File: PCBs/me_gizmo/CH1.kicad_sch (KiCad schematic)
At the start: 10 parts, among them J1 PushButton_Terminal_01x06, U1 ADG714, U2 ADG714, U3 ADG714

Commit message: Completed first draft of integrated measurement unit
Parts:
- removed U2: ADG714, Package_SO:TSSOP-24_4.4x7.8mm_P0.65mm, symbol Analog_Switch:ADG714
- added U2: ADG714, Package_SO:TSSOP-24_4.4x7.8mm_P0.65mm, symbol Analog_Switch:ADG714
- J1: footprint WAGO:CONN5_233-505_WAG -> TerminalBlock_WAGO:TerminalBlock_WAGO_233-506_2x06_P2.54mm
- R4, R7, R8: value 348 -> 348Ω
- R5, R6, R9: value 118 -> 118Ω
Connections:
- net ADC1+: now also U3.5 (S); no longer J1.5 (Pin_5), U3.6 (D)
- net ADC1-: now also J1.5 (Pin_5), U3.7 (S); no longer U3.8 (D)
- net HB1+: now also U3.6 (D), U2.19 (D), U2.6 (D); no longer U3.5 (S)
- net HB1-: now also U3.8 (D), U2.17 (D), U2.8 (D); no longer U3.7 (S)
- net at R7.2: now also U2.18 (S)
- net at R6.1: now also U2.7 (S)
- net at R9.1: now also U2.20 (S)
- net at R8.2: now also U2.5 (S)

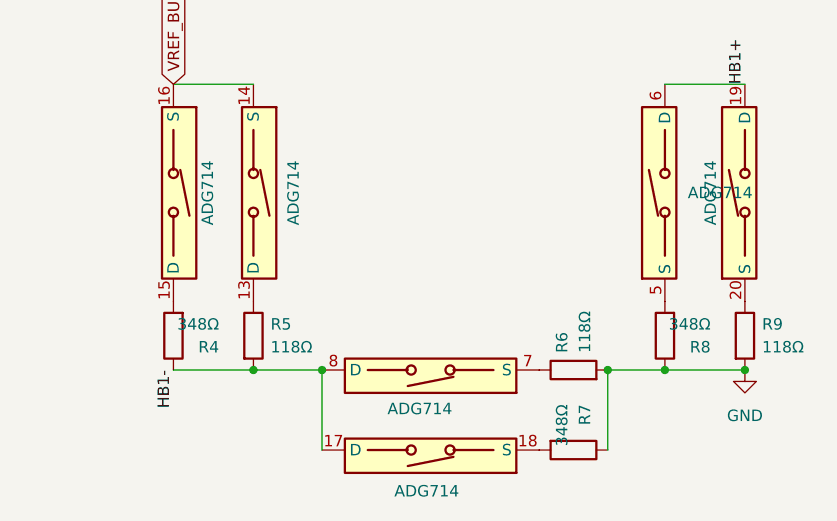
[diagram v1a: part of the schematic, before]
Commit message: Added Main.py with a channel configuration detection script. Also added a thread that updates the leds to display what the device thinks the current operating mode is, particularly while actively looping detect_config. Finally, there are a bunch of untested updates (mostly software) to make the code compatible with the new board. Any replaced working protoype code exists underneath the revisions labeled with 'protptype above it. This commit contains a few key revisions to the hardware including pulling all of the RGB LEDs to ground so that they can be enabled, and pull down resistors on the adc channels that are not connected to the DAC.
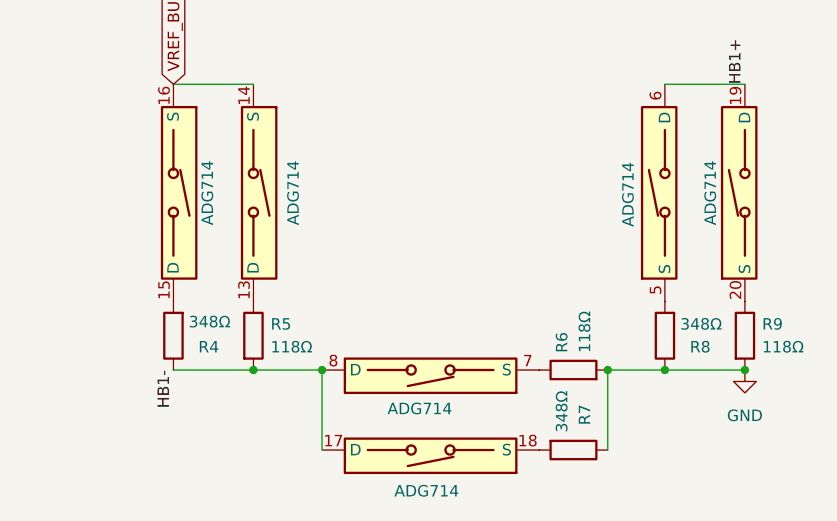
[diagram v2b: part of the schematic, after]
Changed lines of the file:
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@@
 		(on_board yes)
 		(dnp no)
-		(fields_autoplaced yes)
 		(property "Reference" "U2"
 			(at 194.818 99.06 0)
@@
 		)
 		(property "Value" "ADG714"
-			(at 191.77 99.6949 90)
+			(at 185.166 96.266 0)
 			(effects
 				(font
@@
 		)
 		(property "Value" "348Ω"
-			(at 139.7 114.3 0)
+			(at 140.97 114.046 0)
 			(effects
 				(font
@@
 		)
 		(property "Value" "348Ω"
-			(at 177.8 123.19 0)
+			(at 177.8 121.666 0)
 			(effects
 				(font
@@
 		)
 		(property "Value" "348Ω"
-			(at 194.31 114.3 0)
-			(effects
-				(font
+			(at 195.58 114.3 0)
+			(effects
+				(font
